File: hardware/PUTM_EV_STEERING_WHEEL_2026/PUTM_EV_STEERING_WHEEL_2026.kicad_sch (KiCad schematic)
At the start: 0 parts

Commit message: Preview schematic
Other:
- added sheet CAN (can.kicad_sch)
- added sheet CONNECTORS (connectors.kicad_sch)
- added sheet POWER (power.kicad_sch)
- sheet uC ports: added {USART1}; removed POWER

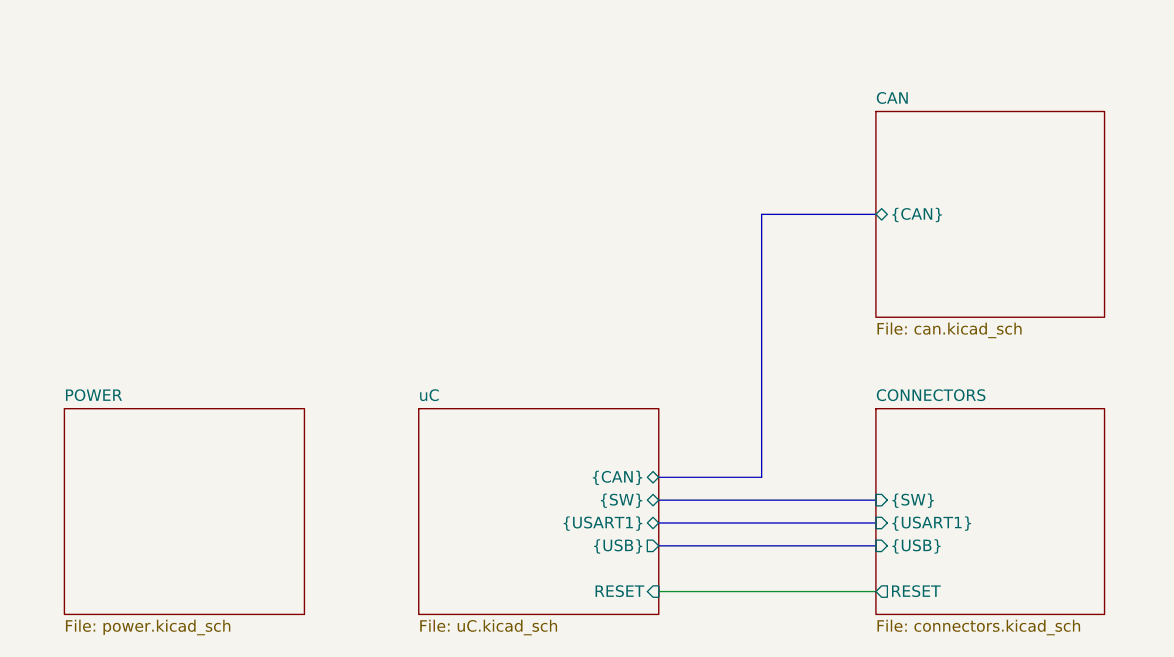
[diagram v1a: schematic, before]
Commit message: Generate code & work on buttons on schematic
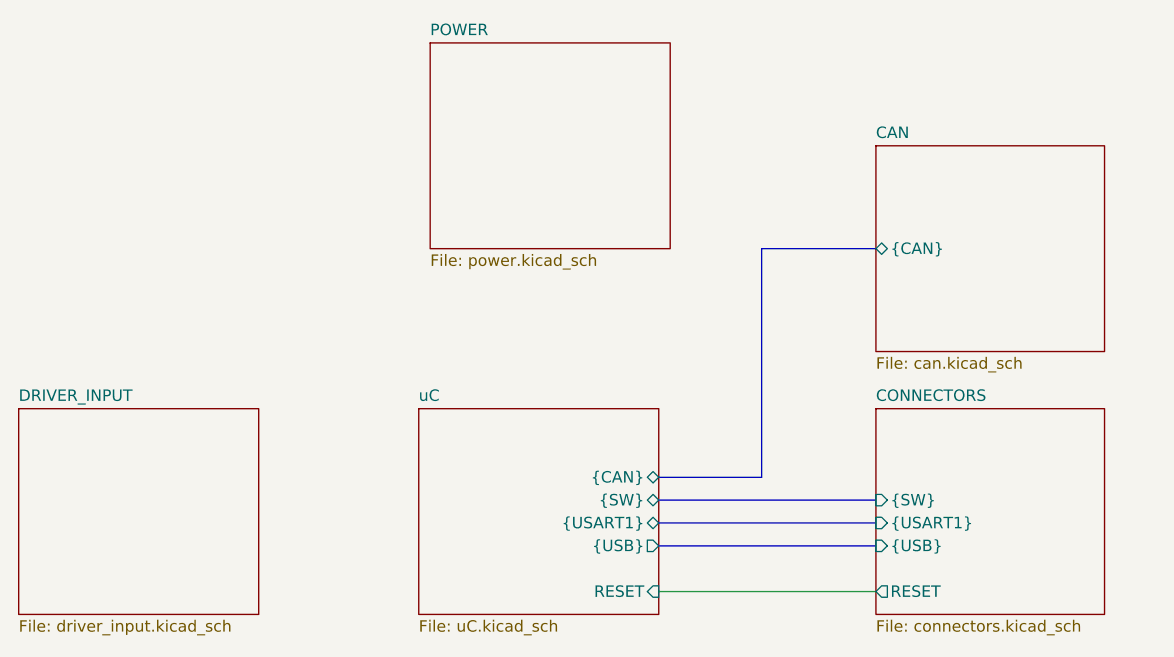
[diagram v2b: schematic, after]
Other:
- added sheet DRIVER_INPUT (driver_input.kicad_sch)
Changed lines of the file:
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@@
 	(bus
 		(pts
-			(xy 166.37 100.33) (xy 166.37 71.12)
+			(xy 166.37 100.33) (xy 166.37 74.93)
 		)
 		(stroke
@@
 	(bus
 		(pts
-			(xy 166.37 71.12) (xy 179.07 71.12)
+			(xy 166.37 74.93) (xy 179.07 74.93)
 		)
 		(stroke
@@
 	)
 	(sheet
-		(at 179.07 59.69)
+		(at 179.07 63.5)
 		(size 25.4 22.86)
 		(exclude_from_sim no)
@@
 		)
 		(property "Sheetname" "CAN"
-			(at 179.07 58.9784 0)
+			(at 179.07 62.7884 0)
 			(effects
 				(font
@@
 		)
 		(property "Sheetfile" "can.kicad_sch"
-			(at 179.07 83.1346 0)
+			(at 179.07 86.9446 0)
 			(effects
 				(font
@@
 		)
 		(pin "{CAN}" bidirectional
-			(at 179.07 71.12 180)
+			(at 179.07 74.93 180)
 			(effects
 				(font
@@
 	)
 	(sheet
-		(at 88.9 92.71)
+		(at 129.54 52.07)
 		(size 26.67 22.86)
 		(exclude_from_sim no)
@@
 		)
 		(property "Sheetname" "POWER"
-			(at 88.9 91.9984 0)
+			(at 129.54 51.3584 0)
 			(effects
 				(font
@@
 		)
 		(property "Sheetfile" "power.kicad_sch"
-			(at 88.9 116.1546 0)
+			(at 129.54 75.5146 0)
 			(effects
 				(font
@@
 				)
 			)
+		)
+	)
+	(sheet
+		(at 83.82 92.71)
+		(size 26.67 22.86)
+		(exclude_from_sim no)
+		(in_bom yes)
+		(on_board yes)
+		(dnp no)
+		(fields_autoplaced yes)
+		(stroke
+			(width 0.1524)
+			(type solid)
+		)
+		(fill
+			(color 0 0 0 0.0000)
+		)
+		(property "Sheetname" "DRIVER_INPUT"
+			(at 83.82 91.9984 0)
+			(effects
+				(font
+					(size 1.27 1.27)
+				)
+				(justify left bottom)
+			)
+		)
+		(property "Sheetfile" "driver_input.kicad_sch"
+			(at 83.82 116.1546 0)
+			(effects
+				(font
+					(size 1.27 1.27)
+				)
+				(justify left top)
+			)
+		)
+		(instances
+			(project "PUTM_EV_STEERING_WHEEL_2026"
+				(path "/b652b05a-4e3d-4ad1-b032-18886abe7d45"
+					(page "6")
+				)
+			)
